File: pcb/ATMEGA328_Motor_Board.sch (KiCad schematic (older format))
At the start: 0 parts

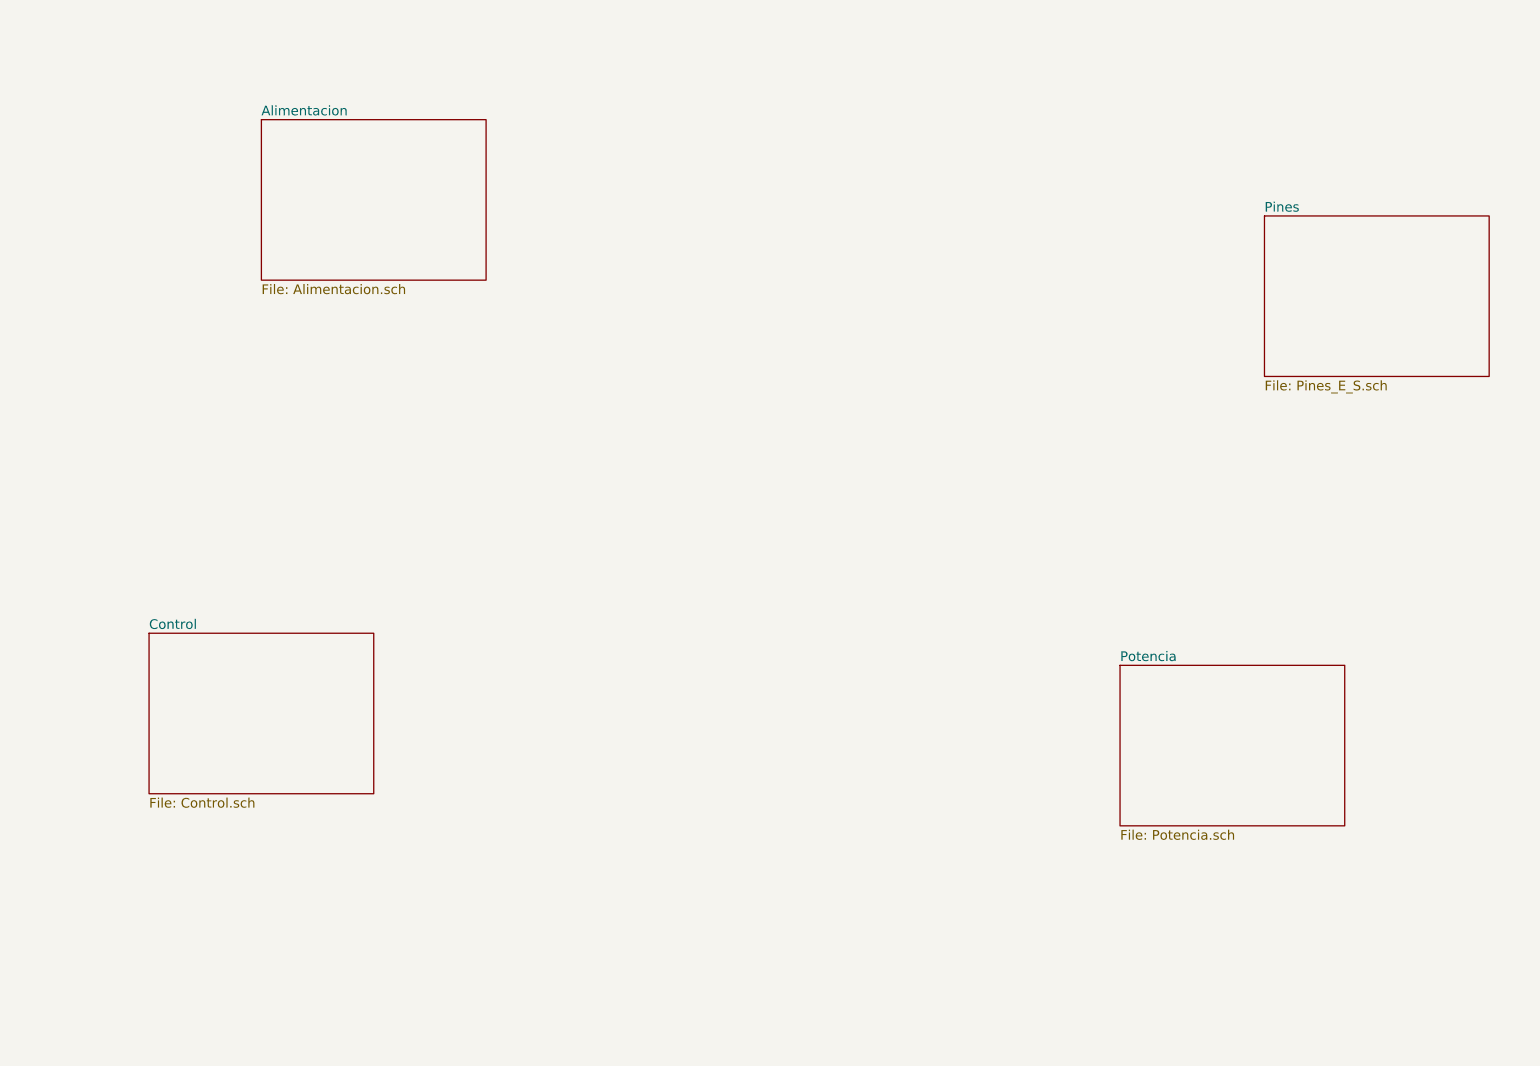
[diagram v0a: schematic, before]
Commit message: carga de hojas jerarquia
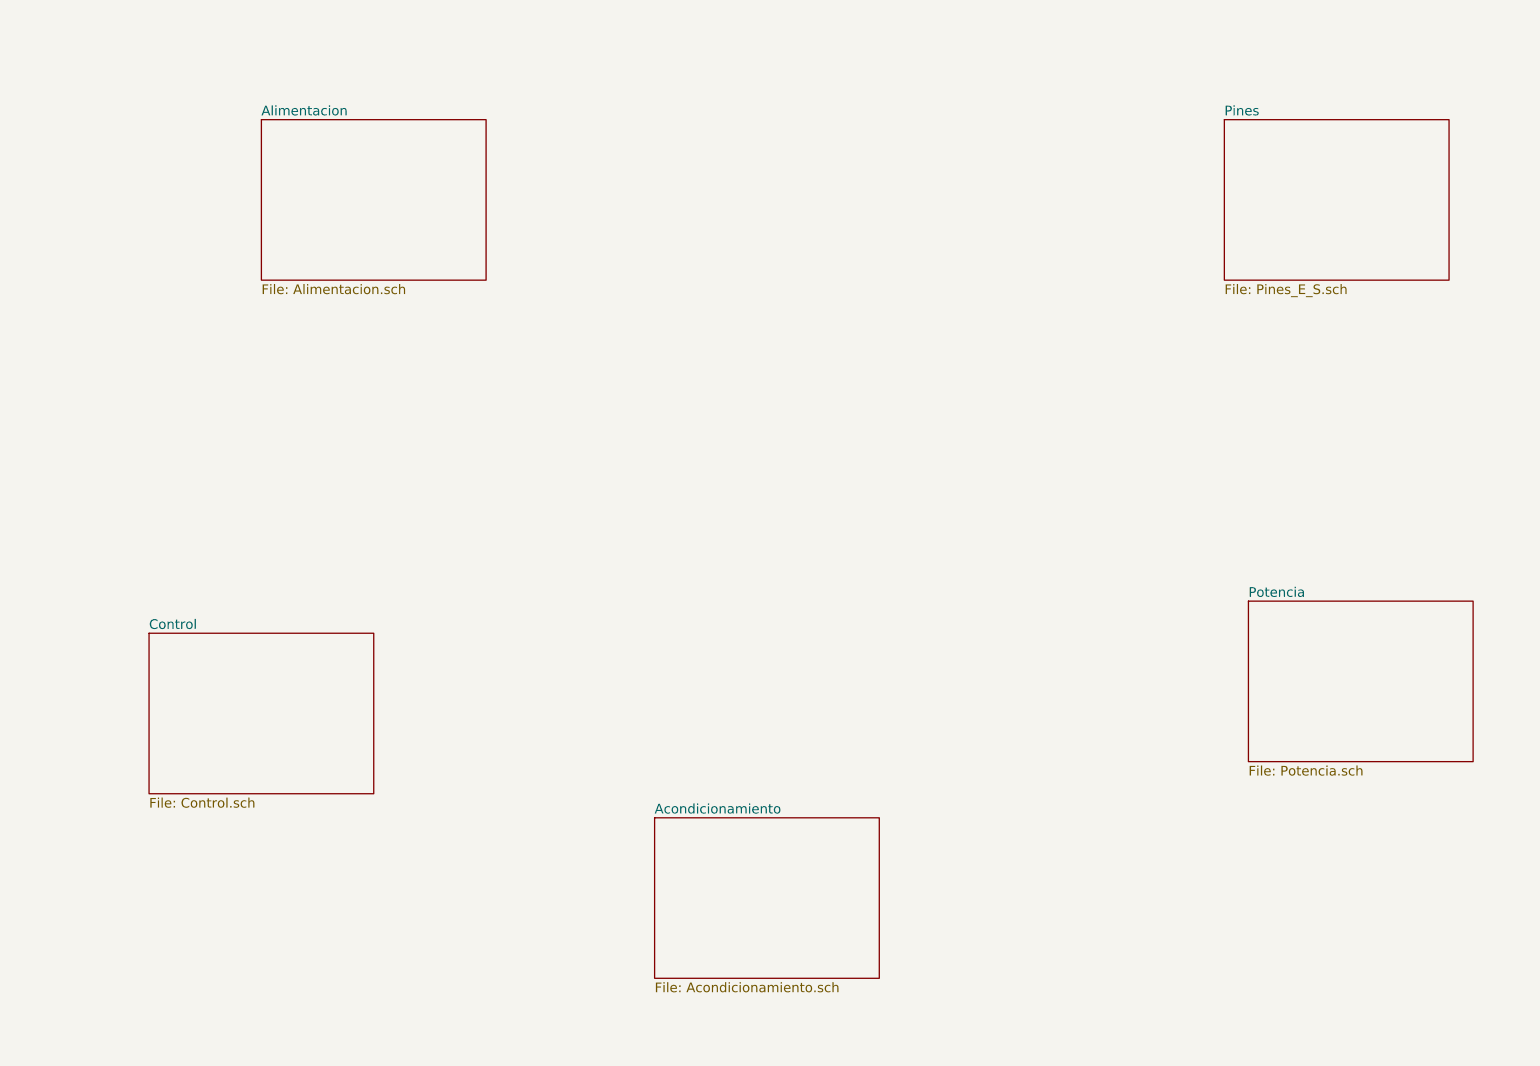
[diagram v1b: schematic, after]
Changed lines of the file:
@@
 EESchema Schematic File Version 2
+LIBS:ATMEGA328_Motor_Board-rescue
 LIBS:Microcontroladores
 LIBS:power
@@
 LIBS:MotorDrivers
 LIBS:connector
+LIBS:Opamp
 LIBS:ATMEGA328_Motor_Board-cache
 EELAYER 25 0
@@
 $Descr A4 11693 8268
 encoding utf-8
-Sheet 1 5
+Sheet 1 6
 Title ""
 Date ""
@@
 $EndSheet
 $Sheet
-S 7650 4900 1400 1000
+S 8450 4500 1400 1000
 U 576895B7
 F0 "Potencia" 60
@@
 $EndSheet
 $Sheet
-S 8550 2100 1400 1000
+S 8300 1500 1400 1000
 U 5768970A
 F0 "Pines" 60
@@
 F1 "Alimentacion.sch" 60
 $EndSheet
+$Sheet
+S 4750 5850 1400 1000
+U 576D539B
+F0 "Acondicionamiento" 60
+F1 "Acondicionamiento.sch" 60
+$EndSheet
 $EndSCHEMATC

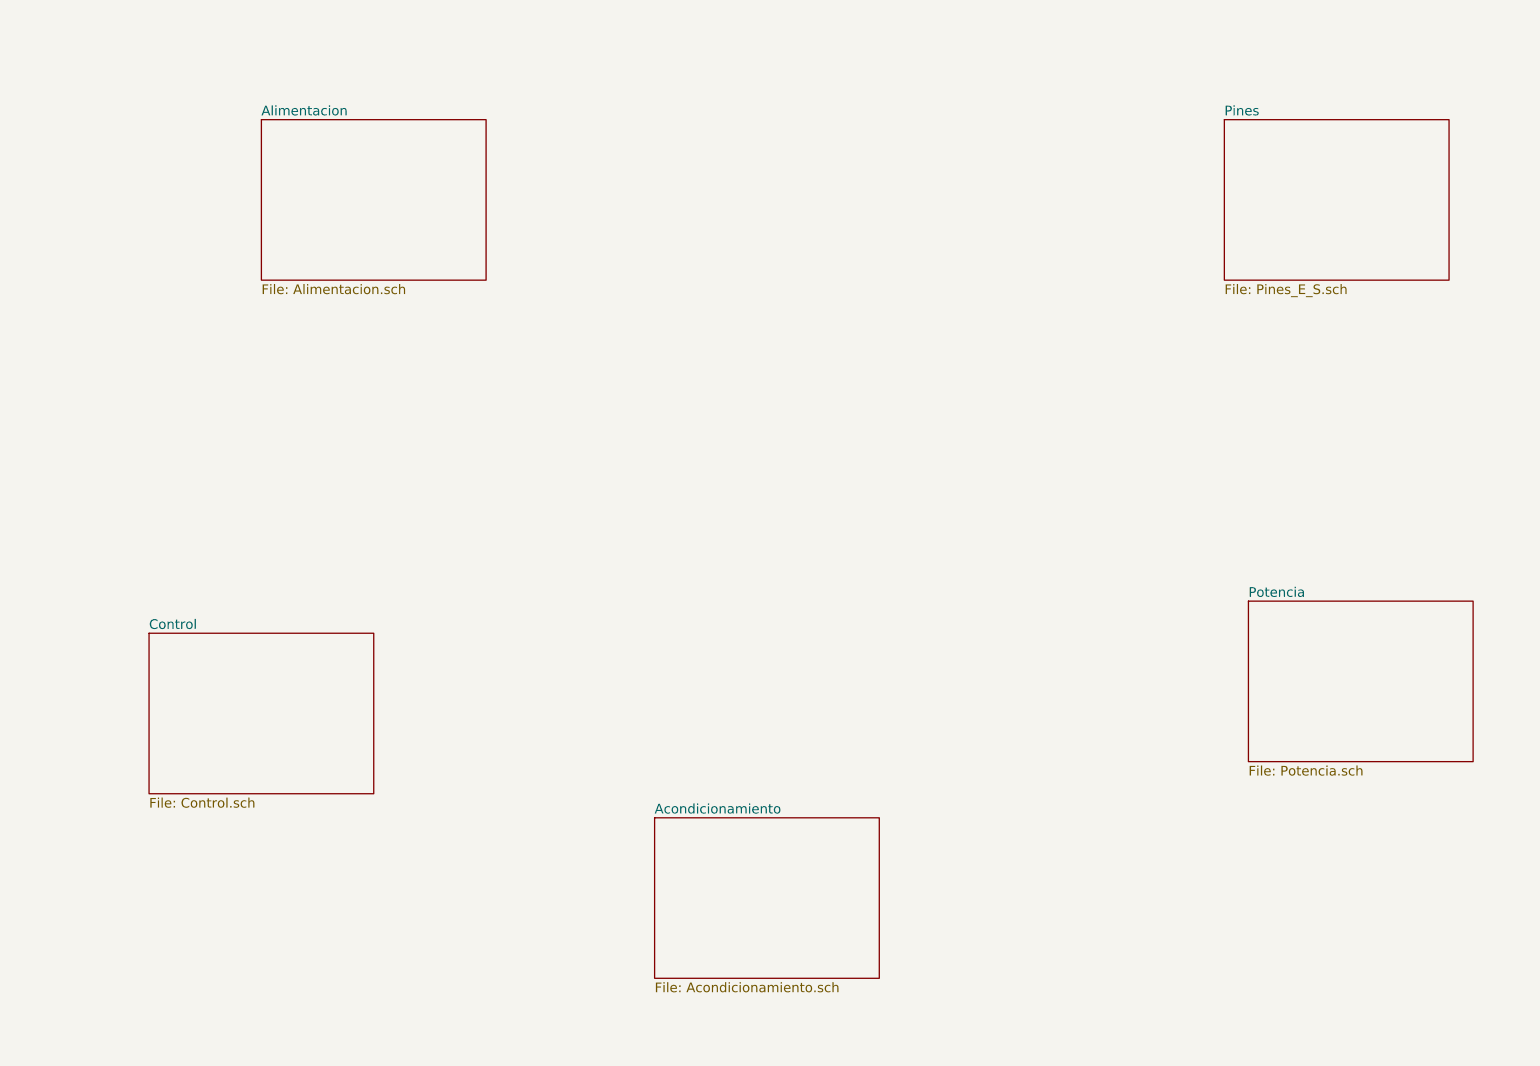
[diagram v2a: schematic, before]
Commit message: se añaden optos para E/S y cristal
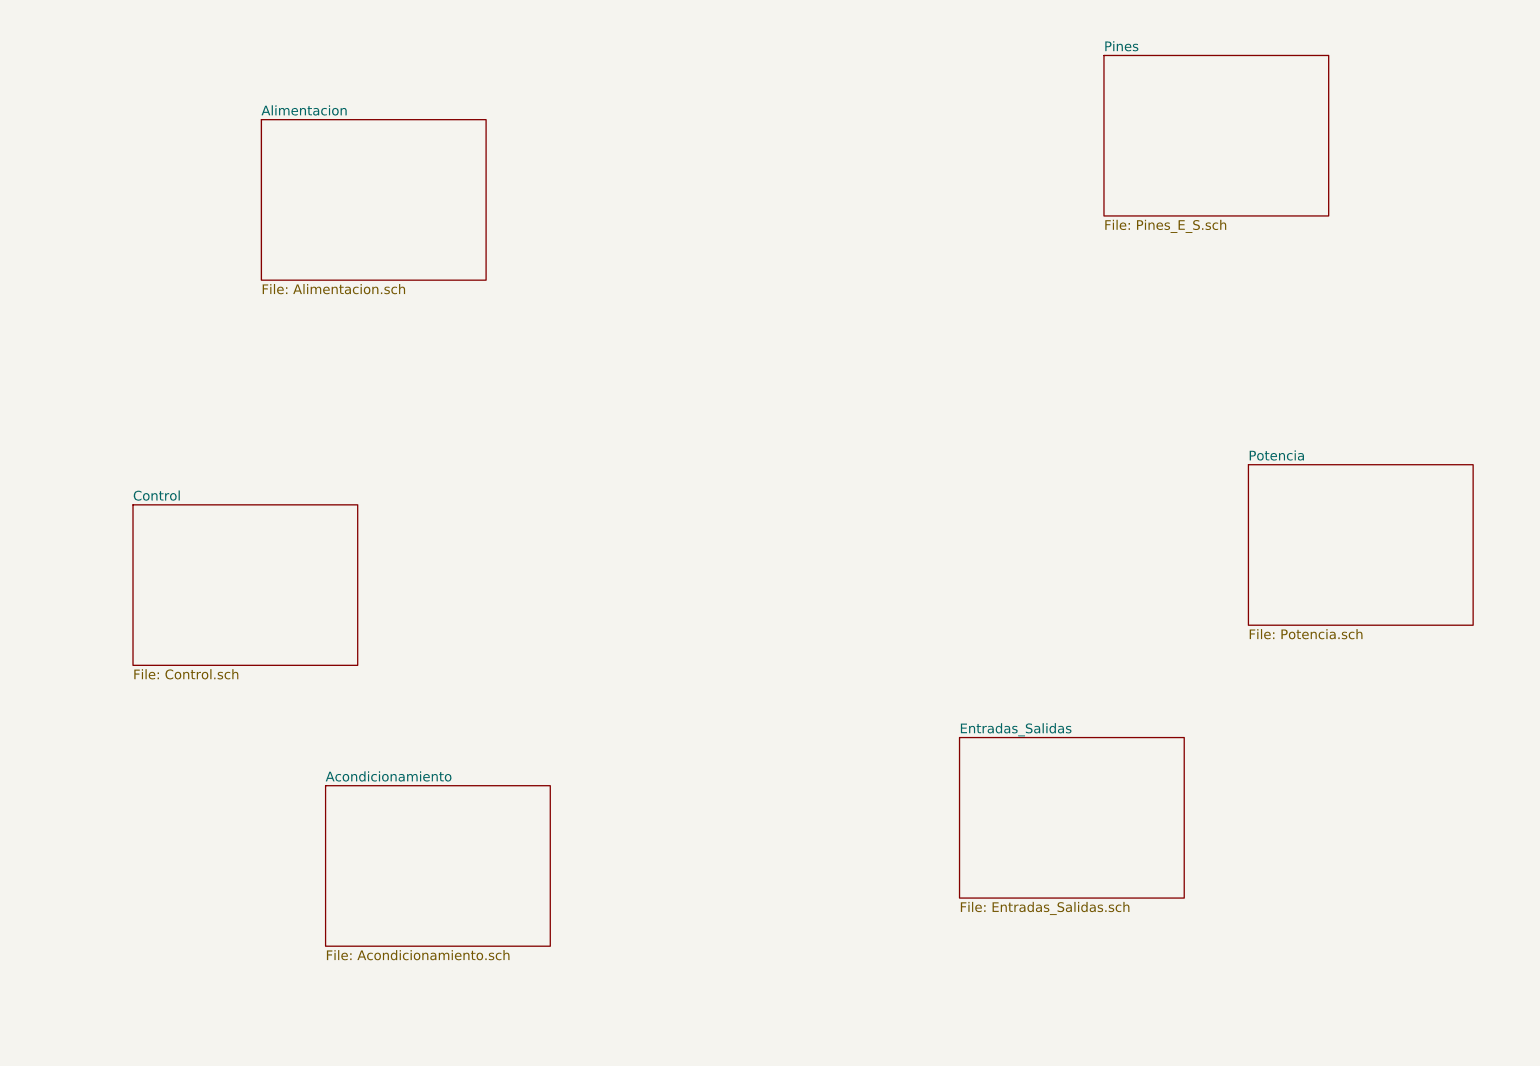
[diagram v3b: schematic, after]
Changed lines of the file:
@@
 LIBS:Opamp
 LIBS:Traco
+LIBS:Optoacoplados
 LIBS:ATMEGA328_Motor_Board-cache
 EELAYER 25 0
@@
 $Descr A4 11693 8268
 encoding utf-8
-Sheet 1 6
+Sheet 1 7
 Title ""
 Date ""
@@
 $EndDescr
 $Sheet
-S 1600 4700 1400 1000
+S 1500 3900 1400 1000
 U 5768938A
 F0 "Control" 60
@@
 $EndSheet
 $Sheet
-S 8450 4500 1400 1000
+S 8450 3650 1400 1000
 U 576895B7
 F0 "Potencia" 60
@@
 $EndSheet
 $Sheet
-S 8300 1500 1400 1000
+S 7550 1100 1400 1000
 U 5768970A
 F0 "Pines" 60
@@
 $EndSheet
 $Sheet
-S 4750 5850 1400 1000
+S 2700 5650 1400 1000
 U 576D539B
 F0 "Acondicionamiento" 60
 F1 "Acondicionamiento.sch" 60
 $EndSheet
+$Sheet
+S 6650 5350 1400 1000
+U 57841AC1
+F0 "Entradas_Salidas" 60
+F1 "Entradas_Salidas.sch" 60
+$EndSheet
 $EndSCHEMATC

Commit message: añadir imagenes y datos al esquema electrico
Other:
- note added: "Este diseño es Software Libre; usted puede redistribuirlo y/o modificarlo bajo los términos\nde la "GNU General Public License" como lo publica la "FSF Free Software Foundation",\no (a su elección) de cualquier versión posterior.\n\nEste diseño es distribuido con la esperanza de que le sea útil, pero SIN NINGUNA GARANTIA; \nincluso sin la garantía implícita por la VENTA o EJERCICIO DE ALGUN PROPO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"
